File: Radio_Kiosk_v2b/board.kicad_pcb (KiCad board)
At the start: 2 copper layers, 84 x 133 mm, 239 parts, among them J1 USB-C PD in, J11 UART, J12 USB-C, J13 Lid LEDs, J2 DC in 18-26V, PJ-002BH 5.5x2.5, J3 Laptop out 15.6V, PJ-002BH 5.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, J5 RJ45 radio, J6 RJ45 laptop, J8 Fan 12V, J9 SWD, Q1 SI4470EY, Q10 2N7002, Q11 AO3400A, Q12 SI4470EY, Q13 AO4482, Q2 SI4470EY, Q20 AO4482, Q22 PSMN075-100MSEX, Q23 DMP10H400SE, Q24 BSS123, Q25 2N7002, Q30 AO3400A, Q40 AOD4184A, Q41 AOD4184A, Q44 SI4401DDY, Q45 2N7002, Q6 SI4470EY, Q7 SI4470EY, Q8 AOD4185, Q9 2N7002, SW1 RESET, SW2 BOOT0 (DFU), U1 LM74700-Q1, U10 TLV7011, U12 LM74700-Q1, U2 LM74700-Q1, U20 LM3478 54V boost, U21 TPS26600 eFuse, U22 LTC4279, U3 LMR33630 12V, U30 SN74AHCT1G125, U31 SN74AHCT1G125, U4 LM3150 15.75V 4.5A, U40 STM32F072CBT6, U41 INA180A1, U42 INA180A1, U43 MCP6001T-I/OT, U45 TLV7011, U5 LMR33630 5V, U50 CH224A, U51 AP2112K-3.3, U52 USBLC6-2SC6, U6 LM74700-Q1, U7 LM74700-Q1

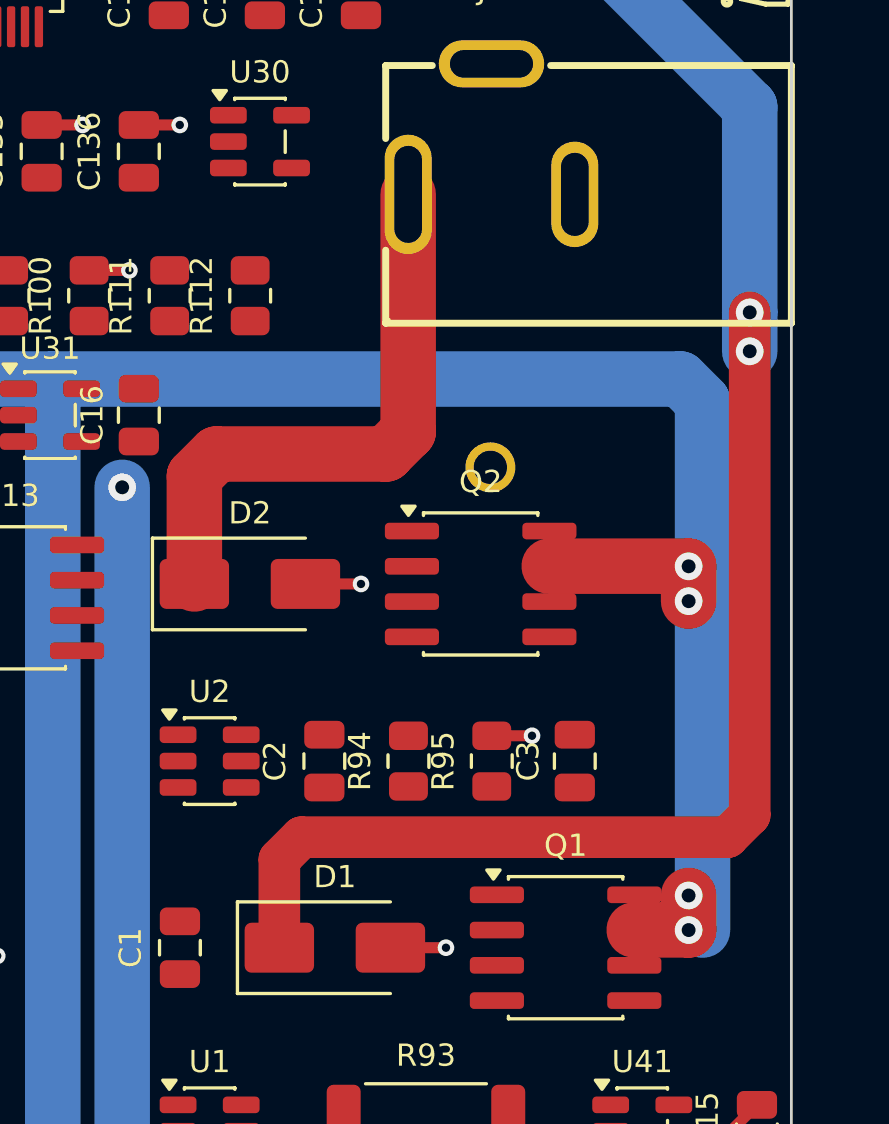
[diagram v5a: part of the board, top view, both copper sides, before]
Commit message: v2b: input stubs back to 1.5 mm; Q1/Q2 sources joined to their input runs
Co-Authored-By: Claude Fable 5.1 <noreply@anthropic.com>
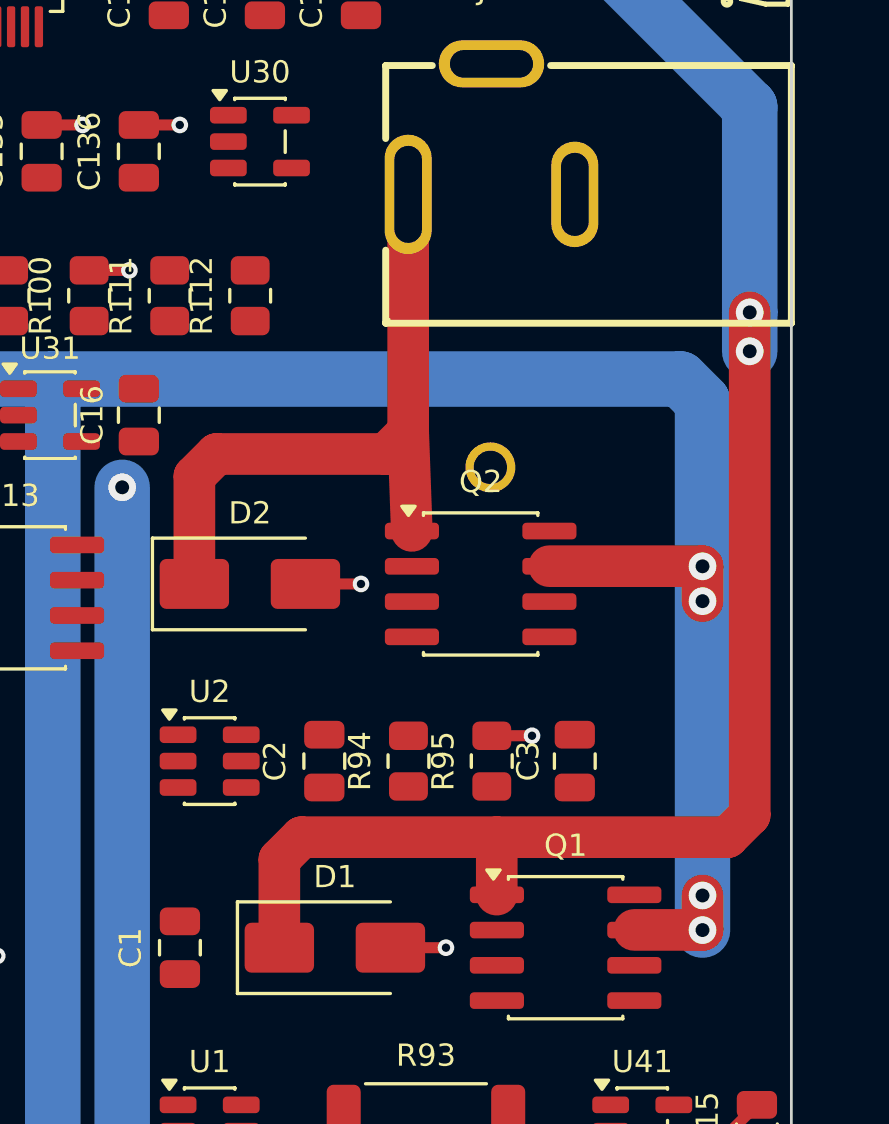
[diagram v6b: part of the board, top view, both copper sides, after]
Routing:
- net VIN_DC: track 20.8 -> 24.4 mm
- net VIN_USB: track 72.9 -> 75.0 mm
- net VIN: track 129.4 -> 130.4 mm
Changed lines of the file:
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@@
 		(start 70.2 38.9)
 		(end 69.4 39.7)
-		(width 2)
+		(width 1.5)
 		(layer "F.Cu")
 		(net "VIN_DC")
@@
 		(start 63.3 39.7)
 		(end 62.5 40.5)
-		(width 2)
+		(width 1.5)
 		(layer "F.Cu")
 		(net "VIN_DC")
@@
 		(start 69.4 39.7)
 		(end 63.3 39.7)
-		(width 2)
+		(width 1.5)
 		(layer "F.Cu")
 		(net "VIN_DC")
@@
 		(start 62.5 40.5)
 		(end 62.5 44.38)
-		(width 2)
+		(width 1.5)
 		(layer "F.Cu")
 		(net "VIN_DC")
@@
 		(start 70.2 30.35)
 		(end 70.2 38.9)
-		(width 2)
+		(width 1.5)
 		(layer "F.Cu")
 		(net "VIN_DC")
@@
 	(segment
 		(start 75.28 43.74)
-		(end 80.3 43.74)
-		(width 2)
+		(end 80.8 43.74)
+		(width 1.5)
 		(layer "F.Cu")
 		(net "VIN")
 	)
 	(segment
-		(start 80.3 56.84)
-		(end 80.3 55.6)
-		(width 2)
+		(start 80.8 56.84)
+		(end 80.8 55.6)
+		(width 1.5)
 		(layer "F.Cu")
 		(net "VIN")
 	)
 	(segment
-		(start 80.3 43.74)
-		(end 80.3 45)
-		(width 2)
+		(start 80.8 43.74)
+		(end 80.8 45)
+		(width 1.5)
 		(layer "F.Cu")
 		(net "VIN")
@@
 	(segment
 		(start 78.34 56.84)
-		(end 80.3 56.84)
-		(width 2)
+		(end 80.8 56.84)
+		(width 1.5)
 		(layer "F.Cu")
 		(net "VIN")
@@
 	)
 	(via
-		(at 80.3 56.845)
+		(at 80.8 56.845)
 		(size 1)
 		(drill 0.5)
@@
 	)
 	(via
-		(at 80.3 55.6)
+		(at 80.8 55.6)
 		(size 1)
 		(drill 0.5)
@@
 	)
 	(via
-		(at 80.3 43.745)
+		(at 80.8 43.745)
 		(size 1)
 		(drill 0.5)
@@
 	)
 	(via
-		(at 80.3 45)
+		(at 80.8 45)
 		(size 1)
 		(drill 0.5)
@@
 		(net "VIN_USB")
 	)
+	(segment
+		(start 70.2 38.9)
+		(end 70.33 42.47)
+		(width 1.5)
+		(layer "F.Cu")
+		(net "VIN_DC")
+	)
+	(segment
+		(start 73.39 53.5)
+		(end 73.39 55.57)
+		(width 1.5)
+		(layer "F.Cu")
+		(net "VIN_USB")
+	)

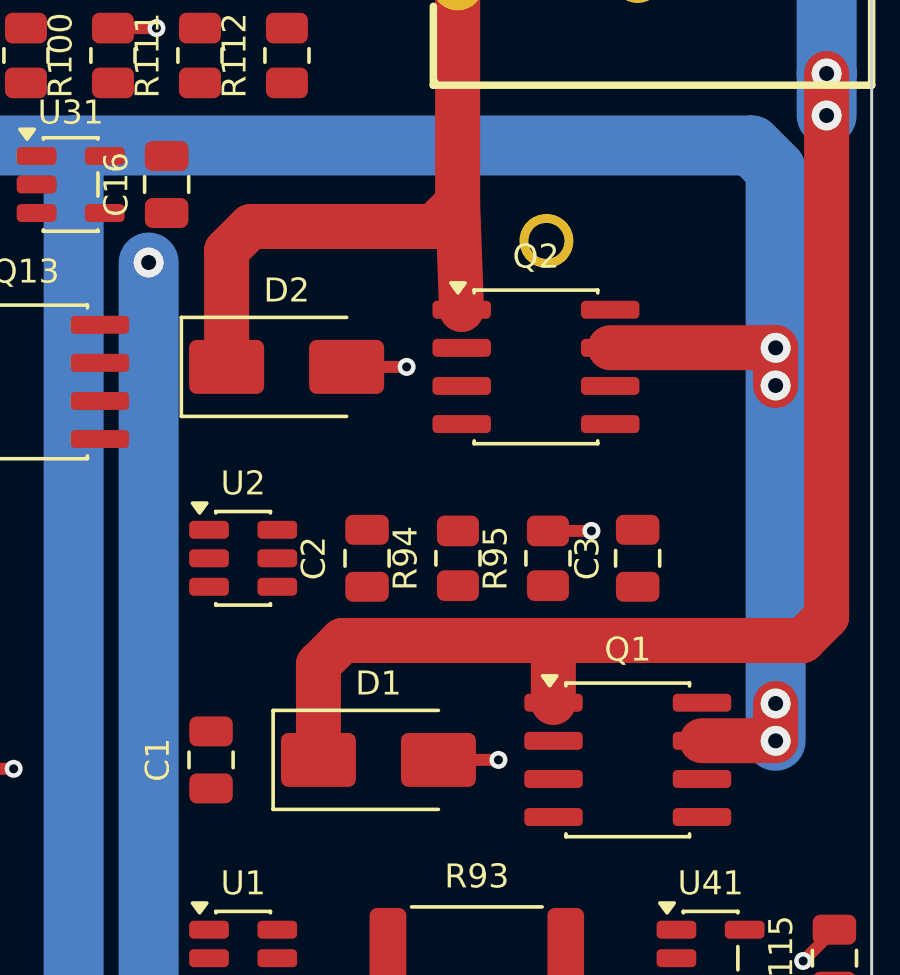
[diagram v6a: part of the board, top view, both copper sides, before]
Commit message: v2b: library names back on 49 footprints, TVS returns at feed width, two wrong stubs removed
49 footprints written by the update script had lost their library nickname
(TO-252-2 instead of Package_TO_SOT_SMD:TO-252-2); KiCad drew them from the
embedded copy but loon could not resolve them and drew stand-ins, and
Update PCB would have flagged them all. D1/D2 ground returns: 0.4 mm to one
via -> 1.5 mm with two vias into the back pour. Removed the VIN_DC and
VIN_USB stubs added at 14:36 (the VIN_USB one shorted Q1). tools/verify.py
checks every footprint's pads against its library and every schematic
part present once.

Co-Authored-By: Claude Opus 5.5 (1M context) <noreply@anthropic.com>
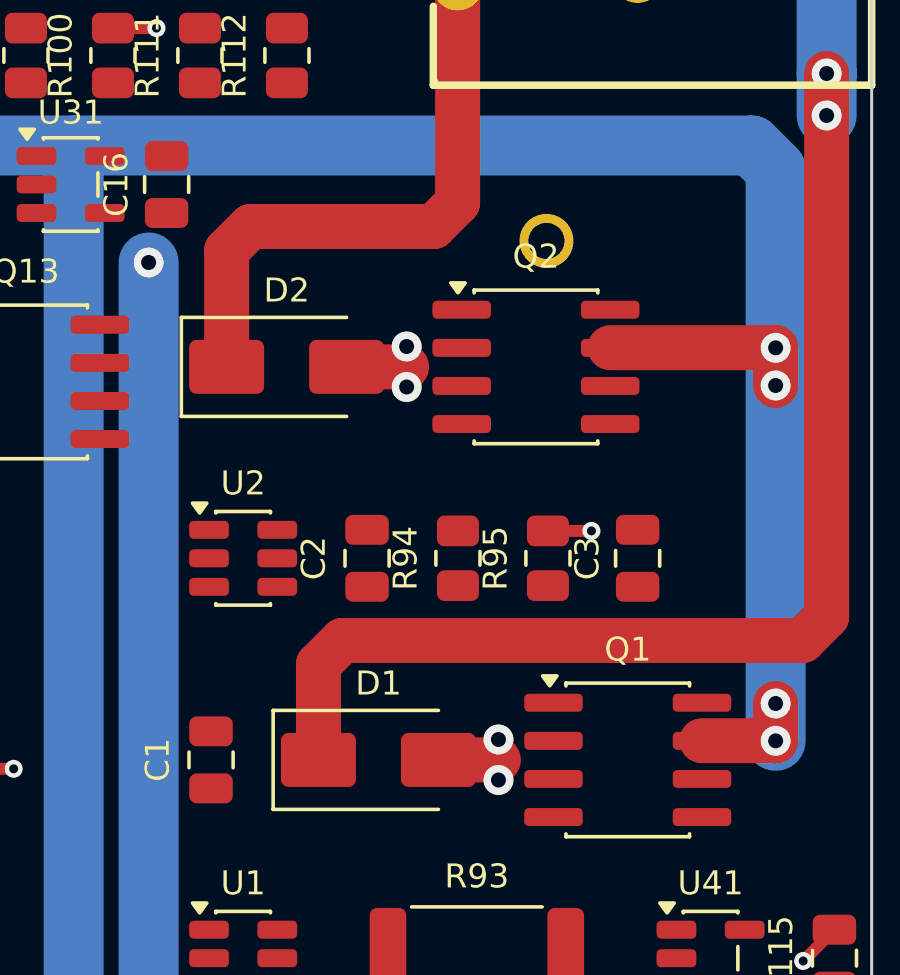
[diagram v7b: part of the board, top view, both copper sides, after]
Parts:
- C119, C12, C120, C13, C14, C15, C16, C17, C3, C48, C49, C5: footprint C_0805_2012Metric -> Capacitor_SMD:C_0805_2012Metric
- C26: footprint C_1210_3225Metric -> Capacitor_SMD:C_1210_3225Metric
- C4: footprint CP_Elec_8x10.5 -> Capacitor_SMD:CP_Elec_8x10.5
- C46: footprint CP_Elec_6.3x7.7 -> Capacitor_SMD:CP_Elec_6.3x7.7
- C8: footprint C_1206_3216Metric -> Capacitor_SMD:C_1206_3216Metric
- D23: footprint D_SOD-123 -> Diode_SMD:D_SOD-123
- L3, L4: footprint IND-SMD_L10.0-W10.0-APS10A40M470 -> LCSC:IND-SMD_L10.0-W10.0-APS10A40M470
- Q11, Q24, Q25: footprint SOT-23 -> Package_TO_SOT_SMD:SOT-23
- Q12: footprint SOIC-8_3.9x4.9mm_P1.27mm -> Package_SO:SOIC-8_3.9x4.9mm_P1.27mm
- Q23: footprint SOT-223_L6.5-W3.5-P2.30-LS7.0-BR -> LCSC:SOT-223_L6.5-W3.5-P2.30-LS7.0-BR
- Q40, Q41: footprint TO-252-2 -> Package_TO_SOT_SMD:TO-252-2
- R10, R113, R27, R28, R29, R42, R44, R45, R46, R47, R48, R49, R5, R6, R64, R65, R66, R7, R8, R9: footprint R_0805_2012Metric -> Resistor_SMD:R_0805_2012Metric
- U12: footprint SOT-23-6 -> Package_TO_SOT_SMD:SOT-23-6
- U31: footprint SOT-23-5 -> Package_TO_SOT_SMD:SOT-23-5
- U4: footprint HTSSOP-14_L5.0-W4.4-P0.65-LS6.4-BL-EP -> LCSC:HTSSOP-14_L5.0-W4.4-P0.65-LS6.4-BL-EP
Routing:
- net VIN_DC: track 24.4 -> 20.8 mm
- net GND: track 120.6 -> 123.3 mm, vias 73 -> 75
- net VIN_USB: track 75.0 -> 72.9 mm
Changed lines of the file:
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@@
 		)
 	)
-	(footprint "C_1206_3216Metric"
+	(footprint "Capacitor_SMD:C_1206_3216Metric"
 		(layer "F.Cu")
 		(at 18.4 40)
@@
 		)
 	)
-	(footprint "SOT-23"
+	(footprint "Package_TO_SOT_SMD:SOT-23"
 		(layer "F.Cu")
 		(at 21.4 45)
@@
 		)
 	)
-	(footprint "C_0805_2012Metric"
+	(footprint "Capacitor_SMD:C_0805_2012Metric"
 		(layer "F.Cu")
 		(at 9.6 40)
@@
 		)
 	)
-	(footprint "SOT-23"
+	(footprint "Package_TO_SOT_SMD:SOT-23"
 		(layer "F.Cu")
 		(at 55 85.6)
@@
 		(embedded_fonts no)
 	)
-	(footprint "R_0805_2012Metric"
+	(footprint "Resistor_SMD:R_0805_2012Metric"
 		(layer "F.Cu")
 		(at 48.6 39.4 90)
@@
 		)
 	)
-	(footprint "R_0805_2012Metric"
+	(footprint "Resistor_SMD:R_0805_2012Metric"
 		(layer "F.Cu")
 		(at 44.07 20.9 90)
@@
 		)
 	)
-	(footprint "SOT-23-5"
+	(footprint "Package_TO_SOT_SMD:SOT-23-5"
 		(layer "F.Cu")
 		(at 57.3 38.3)
@@
 		)
 	)
-	(footprint "HTSSOP-14_L5.0-W4.4-P0.65-LS6.4-BL-EP"
+	(footprint "LCSC:HTSSOP-14_L5.0-W4.4-P0.65-LS6.4-BL-EP"
 		(layer "F.Cu")
 		(at 13.63 20.9 -90)
@@
 		)
 	)
-	(footprint "R_0805_2012Metric"
+	(footprint "Resistor_SMD:R_0805_2012Metric"
 		(layer "F.Cu")
 		(at 68.1 78)
@@
 		)
 	)
-	(footprint "C_0805_2012Metric"
+	(footprint "Capacitor_SMD:C_0805_2012Metric"
 		(layer "F.Cu")
 		(at 37.7 33.6 90)
@@
 		)
 	)
-	(footprint "C_0805_2012Metric"
+	(footprint "Capacitor_SMD:C_0805_2012Metric"
 		(layer "F.Cu")
 		(at 32.7 57.66 90)
@@
 		)
 	)
-	(footprint "IND-SMD_L10.0-W10.0-APS10A40M470"
+	(footprint "LCSC:IND-SMD_L10.0-W10.0-APS10A40M470"
 		(layer "F.Cu")
 		(at 25.1 30.75)
@@
 		)
 	)
-	(footprint "D_SOD-123"
+	(footprint "Diode_SMD:D_SOD-123"
 		(layer "F.Cu")
 		(at 57 70.5 90)
@@
 		)
 	)
-	(footprint "R_0805_2012Metric"
+	(footprint "Resistor_SMD:R_0805_2012Metric"
 		(layer "F.Cu")
 		(at 51.4 39.4 90)
@@
 		)
 	)
-	(footprint "R_0805_2012Metric"
+	(footprint "Resistor_SMD:R_0805_2012Metric"
 		(layer "F.Cu")
 		(at 19.6 75.2)
@@
 		)
 	)
-	(footprint "IND-SMD_L10.0-W10.0-APS10A40M470"
+	(footprint "LCSC:IND-SMD_L10.0-W10.0-APS10A40M470"
 		(layer "F.Cu")
 		(at 36.2 100.05)
@@
 		)
 	)
-	(footprint "C_0805_2012Metric"
+	(footprint "Capacitor_SMD:C_0805_2012Metric"
 		(layer "F.Cu")
 		(at 60.5 38.3 90)
@@
 		)
 	)
-	(footprint "C_0805_2012Metric"
+	(footprint "Capacitor_SMD:C_0805_2012Metric"
 		(layer "F.Cu")
 		(at 3 47)
@@
 		)
 	)
-	(footprint "C_1210_3225Metric"
+	(footprint "Capacitor_SMD:C_1210_3225Metric"
 		(layer "F.Cu")
 		(at 75.7 88.03 90)
@@
 		)
 	)
-	(footprint "CP_Elec_6.3x7.7"
+	(footprint "Capacitor_SMD:CP_Elec_6.3x7.7"
 		(layer "F.Cu")
 		(at 40.15 28.1)
@@
 		)
 	)
-	(footprint "SOT-23"
+	(footprint "Package_TO_SOT_SMD:SOT-23"
 		(layer "F.Cu")
 		(at 50.7 85.6)
@@
 		)
 	)
-	(footprint "R_0805_2012Metric"
+	(footprint "Resistor_SMD:R_0805_2012Metric"
 		(layer "F.Cu")
 		(at 7 75.2)
@@
 		)
 	)
-	(footprint "C_0805_2012Metric"
+	(footprint "Capacitor_SMD:C_0805_2012Metric"
 		(layer "F.Cu")
 		(at 76.2 50.76 90)
@@
 		)
 	)
-	(footprint "TO-252-2"
+	(footprint "Package_TO_SOT_SMD:TO-252-2"
 		(layer "F.Cu")
 		(at 24.06 20.9)
@@
 		)
 	)
-	(footprint "R_0805_2012Metric"
+	(footprint "Resistor_SMD:R_0805_2012Metric"
 		(layer "F.Cu")
 		(at 45 88.5)
@@
 		)
 	)
-	(footprint "C_0805_2012Metric"
+	(footprint "Capacitor_SMD:C_0805_2012Metric"
 		(layer "F.Cu")
 		(at 26.5 75.2)
@@
 		)
 	)
-	(footprint "C_0805_2012Metric"
+	(footprint "Capacitor_SMD:C_0805_2012Metric"
 		(layer "F.Cu")
 		(at 21.5 57.66 90)
@@
 		)
 	)
-	(footprint "SOT-23-6"
+	(footprint "Package_TO_SOT_SMD:SOT-23-6"
 		(layer "F.Cu")
 		(at 28.6 57.66)
@@
 		)
 	)
-	(footprint "R_0805_2012Metric"
+	(footprint "Resistor_SMD:R_0805_2012Metric"
 		(layer "F.Cu")
 		(at 81 93.5 90)
@@
 		)
 	)
-	(footprint "CP_Elec_8x10.5"
+	(footprint "Capacitor_SMD:CP_Elec_8x10.5"
 		(layer "F.Cu")
 		(at 40 71.8)
@@
 		)
 	)
-	(footprint "R_0805_2012Metric"
+	(footprint "Resistor_SMD:R_0805_2012Metric"
 		(layer "F.Cu")
 		(at 48.2 75.4)
@@
 		)
 	)
-	(footprint "SOIC-8_3.9x4.9mm_P1.27mm"
+	(footprint "Package_SO:SOIC-8_3.9x4.9mm_P1.27mm"
 		(layer "F.Cu")
 		(at 38 57.66)
@@
 		)
 	)
-	(footprint "C_0805_2012Metric"
+	(footprint "Capacitor_SMD:C_0805_2012Metric"
 		(layer "F.Cu")
 		(at 31.4 40)
@@
 		)
 	)
-	(footprint "C_0805_2012Metric"
+	(footprint "Capacitor_SMD:C_0805_2012Metric"
 		(layer "F.Cu")
 		(at 55 88.8)
@@
 		)
 	)
-	(footprint "R_0805_2012Metric"
+	(footprint "Resistor_SMD:R_0805_2012Metric"
 		(layer "F.Cu")
 		(at 52 75.4)
@@
 		)
 	)
-	(footprint "R_0805_2012Metric"
+	(footprint "Resistor_SMD:R_0805_2012Metric"
 		(layer "F.Cu")
 		(at 3 57)
@@
 		)
 	)
-	(footprint "R_0805_2012Metric"
+	(footprint "Resistor_SMD:R_0805_2012Metric"
 		(layer "F.Cu")
 		(at 3.5 54.5)
@@
 		)
 	)
-	(footprint "R_0805_2012Metric"
+	(footprint "Resistor_SMD:R_0805_2012Metric"
 		(layer "F.Cu")
 		(at 3 20)
@@
 		)
 	)
-	(footprint "R_0805_2012Metric"
+	(footprint "Resistor_SMD:R_0805_2012Metric"
 		(layer "F.Cu")
 		(at 3 26)
@@
 		)
 	)
-	(footprint "R_0805_2012Metric"
+	(footprint "Resistor_SMD:R_0805_2012Metric"
 		(layer "F.Cu")
 		(at 59.8 70.5 90)
@@
 		)
 	)
-	(footprint "SOT-223_L6.5-W3.5-P2.30-LS7.0-BR"
+	(footprint "LCSC:SOT-223_L6.5-W3.5-P2.30-LS7.0-BR"
 		(layer "F.Cu")
 		(at 50.6 70.3)
@@
 		)
 	)
-	(footprint "TO-252-2"
+	(footprint "Package_TO_SOT_SMD:TO-252-2"
 		(layer "F.Cu")
 		(at 36.35 20.9)
@@
 		)
 	)
-	(footprint "R_0805_2012Metric"
+	(footprint "Resistor_SMD:R_0805_2012Metric"
 		(layer "F.Cu")
 		(at 17.4 108.25 90)
@@
 		)
 	)
-	(footprint "R_0805_2012Metric"
+	(footprint "Resistor_SMD:R_0805_2012Metric"
 		(layer "F.Cu")
 		(at 47.22 20.9 90)
@@
 		)
 	)
-	(footprint "R_0805_2012Metric"
+	(footprint "Resistor_SMD:R_0805_2012Metric"
 		(layer "F.Cu")
 		(at 31 88.2)
@@
 		)
 	)
-	(footprint "C_0805_2012Metric"
+	(footprint "Capacitor_SMD:C_0805_2012Metric"
 		(layer "F.Cu")
 		(at 24.5 57.66 90)
@@
 		)
 	)
-	(footprint "R_0805_2012Metric"
+	(footprint "Resistor_SMD:R_0805_2012Metric"
 		(layer "F.Cu")
 		(at 20 108.25 90)
@@
 		)
 	)
-	(footprint "R_0805_2012Metric"
+	(footprint "Resistor_SMD:R_0805_2012Metric"
 		(layer "F.Cu")
 		(at 63.9 78)
@@
 		)
 	)
-	(footprint "C_0805_2012Metric"
+	(footprint "Capacitor_SMD:C_0805_2012Metric"
 		(layer "F.Cu")
 		(at 22.6 108.25 90)
@@
 	)
 	(segment
-		(start 66.5 44.38)
-		(end 68.5 44.38)
-		(width 0.4)
-		(layer "F.Cu")
-		(net "GND")
-	)
-	(segment
 		(start 61.58 22)
 		(end 63.055 22)
@@
 	)
 	(segment
-		(start 69.56 57.48)
-		(end 71.56 57.48)
-		(width 0.4)
-		(layer "F.Cu")
-		(net "GND")
-	)
-	(segment
 		(start 68.75 69.905)
 		(end 70.4 69.905)
@@
 	)
 	(via
-		(at 71.56 57.48)
-		(size 0.6)
-		(drill 0.3)
-		(layers "F.Cu" "B.Cu")
-		(net "GND")
-	)
-	(via
 		(at 32.583 108.293)
 		(size 0.6)
@@
 	)
 	(via
-		(at 68.5 44.38)
-		(size 0.6)
-		(drill 0.3)
-		(layers "F.Cu" "B.Cu")
-		(net "GND")
-	)
-	(via
 		(at 49.38 91.118)
 		(size 0.6)
@@
 	)
 	(segment
-		(start 70.2 38.9)
-		(end 70.33 42.47)
+		(start 66.5 44.38)
+		(end 68.5 44.38)
 		(width 1.5)
 		(layer "F.Cu")
-		(net "VIN_DC")
+		(net "GND")
+	)
+	(segment
+		(start 68.5 43.7)
+		(end 68.5 45.05)
+		(width 1)
+		(layer "F.Cu")
+		(net "GND")
+	)
+	(via
+		(at 68.5 43.7)
+		(size 1)
+		(drill 0.5)
+		(layers "F.Cu" "B.Cu")
+		(net "GND")
+	)
+	(via
+		(at 68.5 45.05)
+		(size 1)
+		(drill 0.5)
+		(layers "F.Cu" "B.Cu")
+		(net "GND")
 	)
 	(segment
-		(start 73.39 53.5)
-		(end 73.39 55.57)
+		(start 69.56 57.48)
+		(end 71.56 57.48)
 		(width 1.5)
 		(layer "F.Cu")
-		(net "VIN_USB")
+		(net "GND")
+	)
+	(segment
+		(start 71.56 56.8)
+		(end 71.56 58.15)
+		(width 1)
+		(layer "F.Cu")
+		(net "GND")
+	)
+	(via
+		(at 71.56 56.8)
+		(size 1)
+		(drill 0.5)
+		(layers "F.Cu" "B.Cu")
+		(net "GND")
+	)
+	(via
+		(at 71.56 58.15)
+		(size 1)
+		(drill 0.5)
+		(layers "F.Cu" "B.Cu")
+		(net "GND")
 	)
 	(zone

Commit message: v2b: laptop buck corner re-laid; board 84 x 141 (8 mm band at y 36)
The corner was ~90 % full, so the bypass FET sat on the Ethernet pairs and
U4's RON/SS/FB/EN/ILIM parts ended up 15-30 mm from their pins. An 8 mm band
at y = 36 (the only line crossing no part and only straight vertical
tracks: the four Ethernet runs, VIN_DC, VIN_USB, which just get longer)
gives the room. Everything below moved as one piece.

Power stage: Q40 over Q41, gates facing U4, Q40's source lead over Q41's
tab (short SW), C40/C44 against Q40's tab, L4 under Q41's tab. U4's quiet
parts in pin order on the strip over the Ethernet (quiet only); BST and ILIM
beside U4; CC loop in one cell under U4; output C45/C46/R96/U42/U7/Q7 down
and right; bypass Q44 + gate parts in the new band by the VIN via (moved to
50.2, 45), comparator by the MCU. Stale copper removed (old U4_SW/FB/RON
vias, the LAPTOP_OUT run to the old Q7, GND stitches under moved parts).
Checker and DRC clean. Unrouted: VIN via -> Q40 tab, Q7 -> J3, and the
block's small-signal nets.

Co-Authored-By: Claude Opus 5.5 (1M context) <noreply@anthropic.com>
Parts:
- moved C48 79.8 mm to (6.80, 25.2)
- moved R8 66.6 mm to (67.0, 38.4)
- moved R99 63.7 mm to (11.8, 43.0)
- moved D24 60.3 mm to (62.7, 38.4), turned to 0 degrees
- moved R92 58.6 mm to (3.10, 18.0)
- moved C118 57.4 mm to (16.1, 43.0)
- moved R7 57.0 mm to (58.6, 38.4)
- moved Q45 56.8 mm to (58.6, 41.6)
- moved R46 54.9 mm to (3.10, 20.4)
- moved Q44 54.2 mm to (52.6, 40.0), turned to 180 degrees
- moved U45 53.4 mm to (46.3, 19.0)
- moved R10 53.3 mm to (41.4, 20.0)
- moved R9 52.9 mm to (41.4, 17.6)
- moved C17 49.9 mm to (46.5, 22.6)
- moved R97 46.0 mm to (11.8, 33.4)
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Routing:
- net LAPTOP_OUT: track 49.2 -> 0.00 mm, vias 4 -> 0
- net VIN_USB: track 72.9 -> 80.9 mm
- net VIN_DC: track 20.8 -> 28.8 mm
- net ETH_3: track 182.0 -> 190.0 mm
- net ETH_1: track 164.6 -> 172.6 mm
- net ETH_2: track 164.6 -> 172.6 mm
- net ETH_6: track 179.3 -> 187.3 mm
- net VIN: track 130.4 -> 125.0 mm
- net U4_SW: track 2.10 -> 0.00 mm, vias 2 -> 0
- net GND: vias 75 -> 72
- net U4_RON: vias 1 -> 0
- net U4_FB: vias 1 -> 0
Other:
- board size 84 x 133 mm -> 84 x 141 mm
